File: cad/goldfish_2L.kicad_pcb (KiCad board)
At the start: 4 copper layers, 17.8 x 33 mm, 26 parts, among them J1 USB_C_Receptacle_16P, J3 Conn_01x12, J4 Conn_01x12, J5 Conn_01x05, U1 ATmega32U4-MU, U2 USBLC6-2P6, X1 16MHz

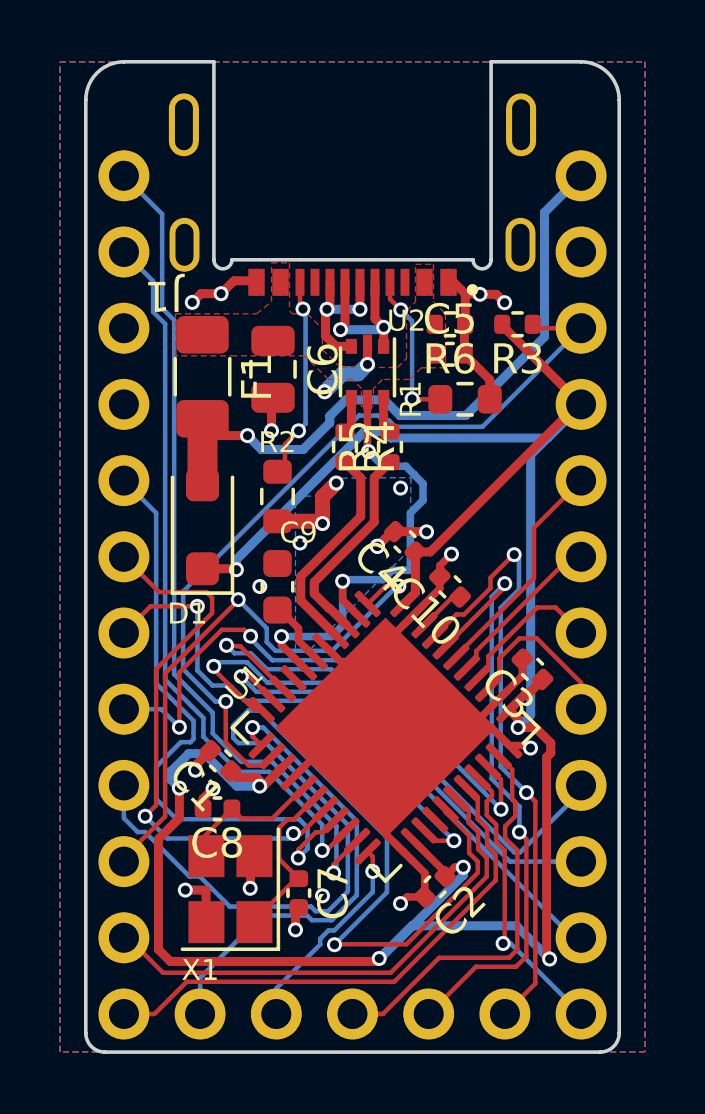
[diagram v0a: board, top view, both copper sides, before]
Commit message: corrected front silkscreens and added schematic PDF files
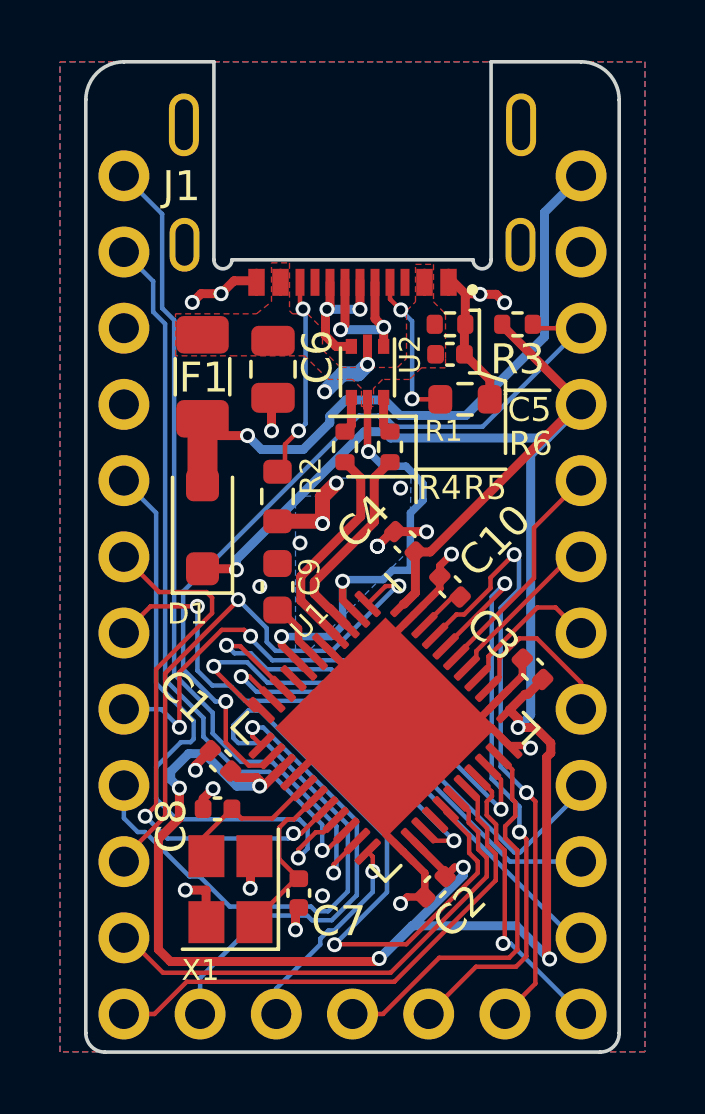
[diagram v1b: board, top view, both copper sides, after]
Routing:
- removed copper zone on In1.Cu, net (none)
- removed copper zone on In2.Cu, net (none)
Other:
- copper layers 4 -> 2
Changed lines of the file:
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@@
   (layers
     (0 "F.Cu" signal)
-    (1 "In1.Cu" power)
-    (2 "In2.Cu" power)
     (31 "B.Cu" signal)
     (32 "B.Adhes" user "B.Adhesive")
@@
       (layer "F.Mask" (type "Top Solder Mask") (color "Green") (thickness 0.01))
       (layer "F.Cu" (type "copper") (thickness 0.035))
-      (layer "dielectric 1" (type "prepreg") (thickness 0.2104) (material "FR4") (epsilon_r 4.5) (loss_tangent 0.02))
-      (layer "In1.Cu" (type "copper") (thickness 0.0152))
-      (layer "dielectric 2" (type "core") (thickness 1.065) (material "FR4") (epsilon_r 4.5) (loss_tangent 0.02))
-      (layer "In2.Cu" (type "copper") (thickness 0.0152))
-      (layer "dielectric 3" (type "prepreg") (thickness 0.2104) (material "FR4") (epsilon_r 4.5) (loss_tangent 0.02))
+      (layer "dielectric 1" (type "core") (thickness 1.5162) (material "FR4") (epsilon_r 4.5) (loss_tangent 0.02))
       (layer "B.Cu" (type "copper") (thickness 0.035))
       (layer "B.Mask" (type "Bottom Solder Mask") (color "Green") (thickness 0.01))
@@
     (property "ki_keywords" "usb universal serial bus type-C USB2.0")
     (attr smd)
-    (fp_text reference "J1" (at 6.3 -5.7 180 unlocked) (layer "F.SilkS")
+    (fp_text reference "J1" (at 5.7 -2.05 unlocked) (layer "F.SilkS")
         (effects (font (size 1 1) (thickness 0.1)))
     )
@@
     (property "ki_keywords" "R res resistor")
     (attr smd)
-    (fp_text reference "R5" (at 0 -1.17 90) (layer "F.SilkS")
-        (effects (font (size 1 1) (thickness 0.15)))
+    (fp_text reference "R5" (at -1.3625 3.17 180) (layer "F.SilkS")
+        (effects (font (size 0.8 0.8) (thickness 0.15)))
     )
     (fp_text value "22R" (at 0 1.17 90) (layer "F.Fab")
@@
     (property "ki_keywords" "cap capacitor")
     (attr smd)
-    (fp_text reference "C1" (at 0 -1.16 135) (layer "F.SilkS")
+    (fp_text reference "C1" (at 2.361737 0.692965 135) (layer "F.SilkS")
         (effects (font (size 1 1) (thickness 0.15)))
     )
@@
     (property "ki_keywords" "R res resistor")
     (attr smd)
-    (fp_text reference "R2" (at 1.8 0) (layer "F.SilkS")
+    (fp_text reference "R2" (at 0.69 1.11 90) (layer "F.SilkS")
         (effects (font (size 0.7 0.7) (thickness 0.125)))
     )
@@
     (property "ki_keywords" "cap capacitor")
     (attr smd)
-    (fp_text reference "C5" (at 0 -1.16) (layer "F.SilkS")
-        (effects (font (size 1 1) (thickness 0.15)))
+    (fp_text reference "C5" (at 2.65 1.85) (layer "F.SilkS")
+        (effects (font (size 0.8 0.8) (thickness 0.15)))
     )
     (fp_text value "100nF" (at 0 1.16) (layer "F.Fab")
@@
     (property "ki_keywords" "cap capacitor")
     (attr smd)
-    (fp_text reference "C8" (at 0 -1.16) (layer "F.SilkS")
+    (fp_text reference "C8" (at 1.54 -0.57 90) (layer "F.SilkS")
         (effects (font (size 1 1) (thickness 0.15)))
     )
@@
     (property "ki_keywords" "AVR 8bit Microcontroller MegaAVR USB")
     (attr smd)
-    (fp_text reference "U1" (at -4.384062 2.262742 225) (layer "F.SilkS")
+    (fp_text reference "U1" (at -4.313351 -0.735391 225) (layer "F.SilkS")
         (effects (font (size 0.7 0.7) (thickness 0.125)))
     )
@@
     (property "ki_keywords" "cap capacitor")
     (attr smd)
-    (fp_text reference "C7" (at 0 -1.16 90) (layer "F.SilkS")
+    (fp_text reference "C7" (at 0.94 -1.33 -180) (layer "F.SilkS")
         (effects (font (size 1 1) (thickness 0.15)))
     )
@@
     (property "ki_keywords" "R res resistor")
     (attr smd)
-    (fp_text reference "R6" (at 0 -1.17) (layer "F.SilkS")
-        (effects (font (size 1 1) (thickness 0.15)))
+    (fp_text reference "R6" (at -2.69 -3.98) (layer "F.SilkS")
+        (effects (font (size 0.8 0.8) (thickness 0.15)))
     )
     (fp_text value "10k" (at 0 1.17) (layer "F.Fab")
@@
     (property "ki_keywords" "resettable fuse PTC PPTC polyfuse polyswitch")
     (attr smd)
-    (fp_text reference "F1" (at 0 -1.82 -90) (layer "F.SilkS")
+    (fp_text reference "F1" (at 0.03 -0.04) (layer "F.SilkS")
         (effects (font (size 1 1) (thickness 0.15)))
     )
@@
     (property "ki_keywords" "cap capacitor")
     (attr smd)
-    (fp_text reference "C3" (at 0 -1.16 135) (layer "F.SilkS")
+    (fp_text reference "C3" (at 1.753625 -0.113137 135) (layer "F.SilkS")
         (effects (font (size 1 1) (thickness 0.15)))
     )
@@
     (property "ki_keywords" "cap capacitor")
     (attr smd)
-    (fp_text reference "C4" (at 0 -1.16 135) (layer "F.SilkS")
+    (fp_text reference "C4" (at 1.449569 -0.516188 225) (layer "F.SilkS")
         (effects (font (size 1 1) (thickness 0.15)))
     )
@@
     (property "ki_keywords" "cap capacitor")
     (attr smd)
-    (fp_text reference "C9" (at 1.8 0.7) (layer "F.SilkS")
+    (fp_text reference "C9" (at 0.33 1.07 90) (layer "F.SilkS")
         (effects (font (size 0.7 0.7) (thickness 0.125)))
     )
@@
     (property "ki_keywords" "usb ethernet video")
     (attr smd)
-    (fp_text reference "U2" (at -1.7 -1.3 180) (layer "F.SilkS")
+    (fp_text reference "U2" (at -0.5875 -1.42 -90) (layer "F.SilkS")
         (effects (font (size 0.7 0.7) (thickness 0.125)))
     )
@@
     (property "ki_keywords" "cap capacitor")
     (attr smd)
-    (fp_text reference "C6" (at 0 -1.68 90) (layer "F.SilkS")
+    (fp_text reference "C6" (at -0.41 -1.48 90) (layer "F.SilkS")
         (effects (font (size 1 1) (thickness 0.15)))
     )
@@
     (property "ki_keywords" "R res resistor")
     (attr smd)
-    (fp_text reference "R1" (at -1.8 0 90) (layer "F.SilkS")
+    (fp_text reference "R1" (at -0.71 1.06 180) (layer "F.SilkS")
         (effects (font (size 0.7 0.7) (thickness 0.125)))
     )
@@
     (property "ki_keywords" "R res resistor")
     (attr smd)
-    (fp_text reference "R4" (at 0 -1.17 -90) (layer "F.SilkS")
-        (effects (font (size 1 1) (thickness 0.15)))
+    (fp_text reference "R4" (at 1.3625 -3.16) (layer "F.SilkS")
+        (effects (font (size 0.8 0.8) (thickness 0.15)))
     )
     (fp_text value "22R" (at 0 1.17 -90) (layer "F.Fab")
@@
     (property "ki_keywords" "cap capacitor")
     (attr smd)
-    (fp_text reference "C10" (at 0 -1.16 135) (layer "F.SilkS")
+    (fp_text reference "C10" (at 0.028284 2.135462 45) (layer "F.SilkS")
         (effects (font (size 1 1) (thickness 0.15)))
     )
@@
       (stroke (width 0.01) (type solid)) (fill solid) (layer "B.SilkS"))
   )
+  (gr_line (start 35.1 34.15) (end 34.23 33.87)
+    (stroke (width 0.12) (type default)) (layer "F.SilkS"))
+  (gr_line (start 32.12 35.46) (end 32.12 35.32)
+    (stroke (width 0.12) (type default)) (layer "F.SilkS"))
+  (gr_line (start 32.12 38.19) (end 32.12 37.08)
+    (stroke (width 0.12) (type default)) (layer "F.SilkS"))
+  (gr_line (start 34.23 33.87) (end 34.23 31.78)
+    (stroke (width 0.12) (type default)) (layer "F.SilkS"))
+  (gr_line (start 35.1 36.55) (end 35.1 34.58)
+    (stroke (width 0.12) (type default)) (layer "F.SilkS"))
+  (gr_line (start 35.1 34.58) (end 35.1 34.45)
+    (stroke (width 0.12) (type default)) (layer "F.SilkS"))
+  (gr_line (start 34.23 33.87) (end 33.9 33.87)
+    (stroke (width 0.12) (type default)) (layer "F.SilkS"))
+  (gr_line (start 32.12 37.08) (end 35.11 37.08)
+    (stroke (width 0.12) (type default)) (layer "F.SilkS"))
+  (gr_line (start 32.1 37.33) (end 29.84 37.33)
+    (stroke (width 0.12) (type default)) (layer "F.SilkS"))
+  (gr_line (start 35.1 34.45) (end 36.58 34.45)
+    (stroke (width 0.12) (type default)) (layer "F.SilkS"))
+  (gr_line (start 32.12 37.08) (end 32.12 35.46)
+    (stroke (width 0.12) (type default)) (layer "F.SilkS"))
+  (gr_line (start 32.12 35.32) (end 29.24 35.32)
+    (stroke (width 0.12) (type default)) (layer "F.SilkS"))
+  (gr_line (start 34.23 31.78) (end 33.92 31.78)
+    (stroke (width 0.12) (type default)) (layer "F.SilkS"))
+  (gr_line (start 35.1 34.45) (end 35.1 34.15)
+    (stroke (width 0.12) (type default)) (layer "F.SilkS"))
   (gr_arc (start 38.89 55.875) (mid 38.704013 56.324013) (end 38.255 56.51)
     (stroke (width 0.12) (type solid)) (layer "Edge.Cuts"))
@@
   (segment (start 25 35.4) (end 25 37.6) (width 1) (layer "F.Cu") (net 40))
   (via (at 26.5 35.96) (size 0.5) (drill 0.3) (layers "F.Cu" "B.Cu") (net 40))
-  (segment (start 37.62 27.3) (end 37.62 27.648629) (width 0.3) (layer "In2.Cu") (net 40))
   (segment (start 33.78066 35.28934) (end 31.58 35.28934) (width 0.3) (layer "B.Cu") (net 40))
   (segment (start 29.77934 34.77) (end 29.243464 35.305876) (width 0.3) (layer "B.Cu") (net 40))
@@
     (polygon
       (pts
-        (xy 39.75 56.5)
-        (xy 20.25 56.5)
-        (xy 20.25 23.5)
-        (xy 39.75 23.5)
-      )
-    )
-  )
-  (zone (net 0) (net_name "") (layer "In1.Cu") (hatch edge 0.508)
-    (connect_pads (clearance 0.15))
-    (min_thickness 0.15) (filled_areas_thickness no)
-    (fill yes (thermal_gap 0.15) (thermal_bridge_width 0.25) (island_removal_mode 1) (island_area_min 10))
-    (polygon
-      (pts
-        (xy 39.75 56.5)
-        (xy 20.25 56.5)
-        (xy 20.25 23.5)
-        (xy 39.75 23.5)
-      )
-    )
-  )
-  (zone (net 0) (net_name "") (layer "In2.Cu") (name "VCC_INT") (hatch edge 0.508)
-    (connect_pads (clearance 0.15))
-    (min_thickness 0.15) (filled_areas_thickness no)
-    (fill yes (thermal_gap 0.15) (thermal_bridge_width 0.25) (island_removal_mode 1) (island_area_min 10))
-    (polygon
-      (pts
